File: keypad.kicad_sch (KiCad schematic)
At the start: 84 parts, among them J1 UJ20-C-H-G-SMT-5-P16-TR, SW1 SW_SPST, SW10 SW_SPST, SW11 SW_SPST, SW12 SW_SPST, SW13 SW_SPST, SW14 SW_SPST, SW15 SW_SPST, SW16 SW_SPST, SW17 SW_SPST, SW18 SW_SPST, SW19 SW_SPST, SW2 SW_SPST, SW20 SW_SPST, SW21 SW_SPST, SW22 SW_SPST, SW23 SW_SPST, SW24 SW_SPST, SW25 SW_SPST, SW26 SW_Reset, SW3 SW_SPST, SW4 SW_SPST, SW5 SW_SPST, SW6 SW_SPST, SW7 SW_SPST, SW8 SW_SPST, SW9 SW_SPST, U1 ATmega32U4-A, Y1 LFXTAL085842

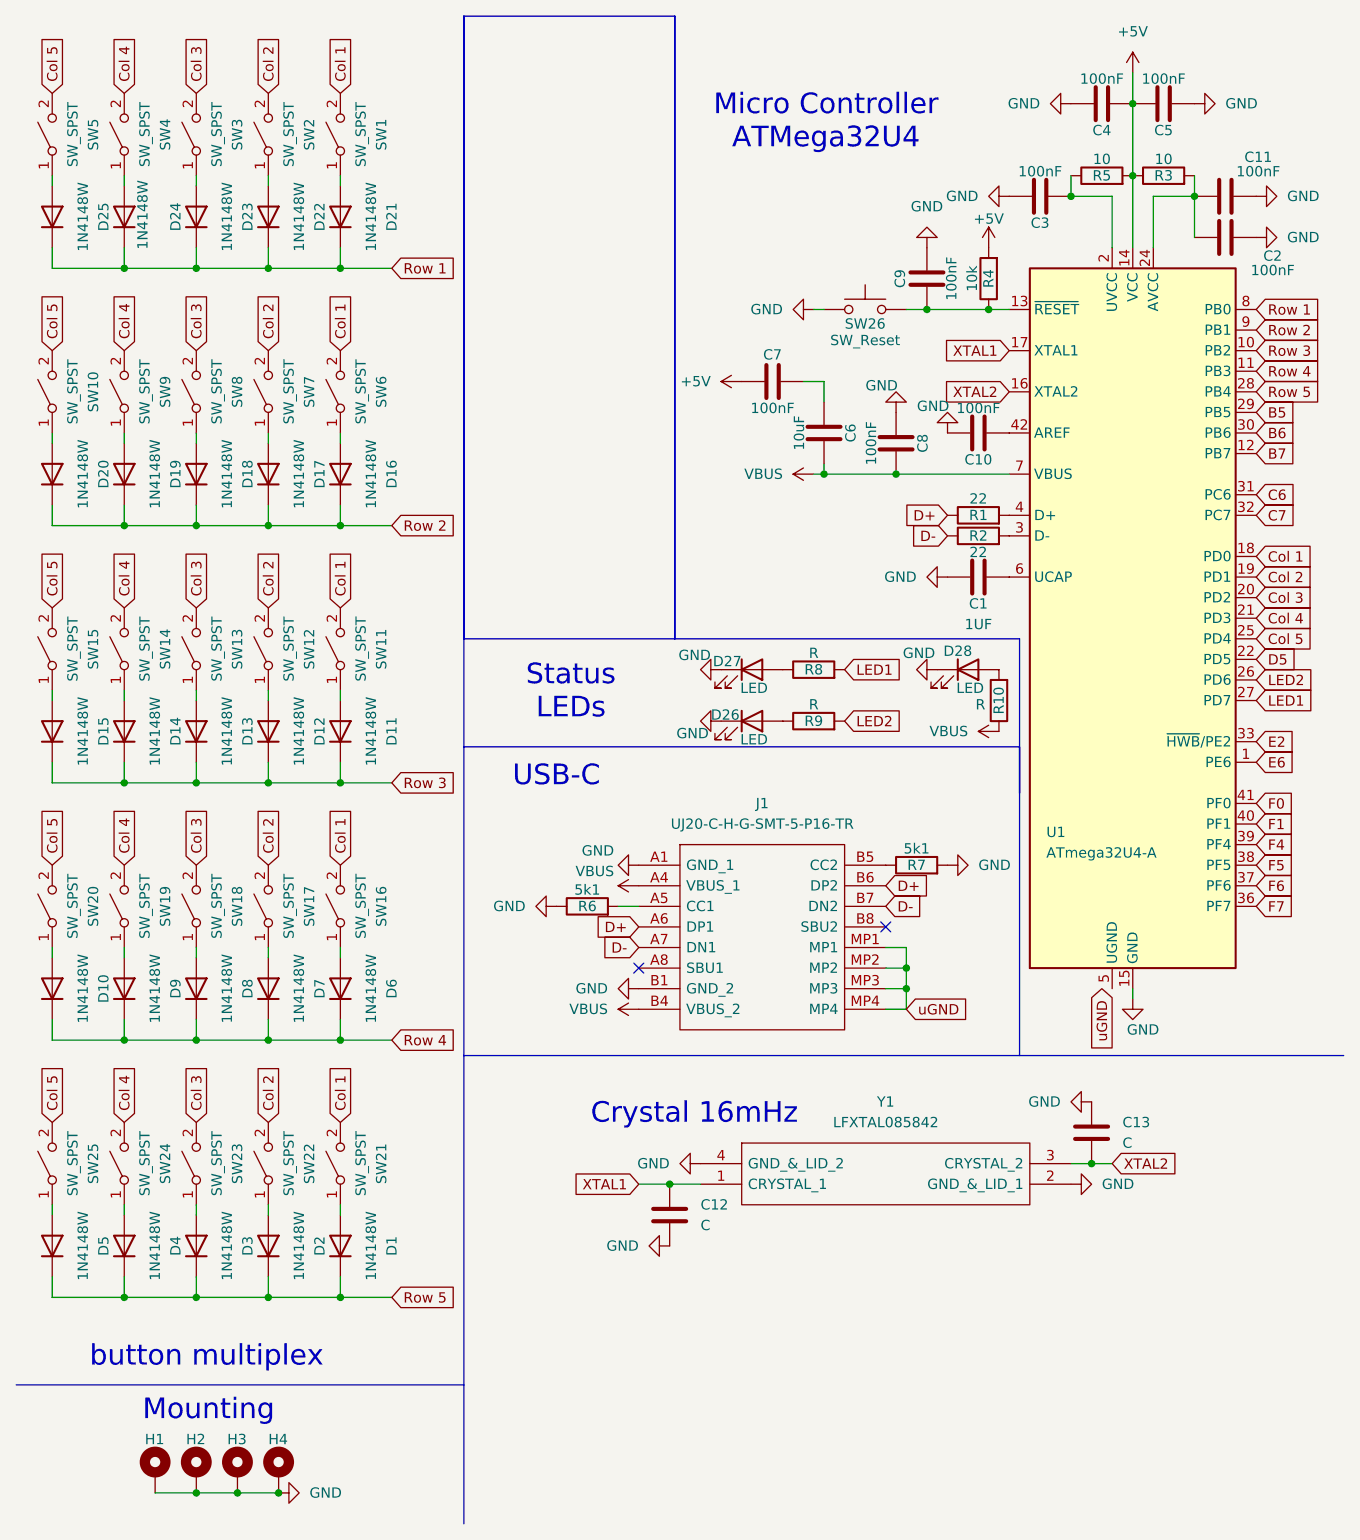
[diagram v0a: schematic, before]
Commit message: switched MC to QFN, rerouted board
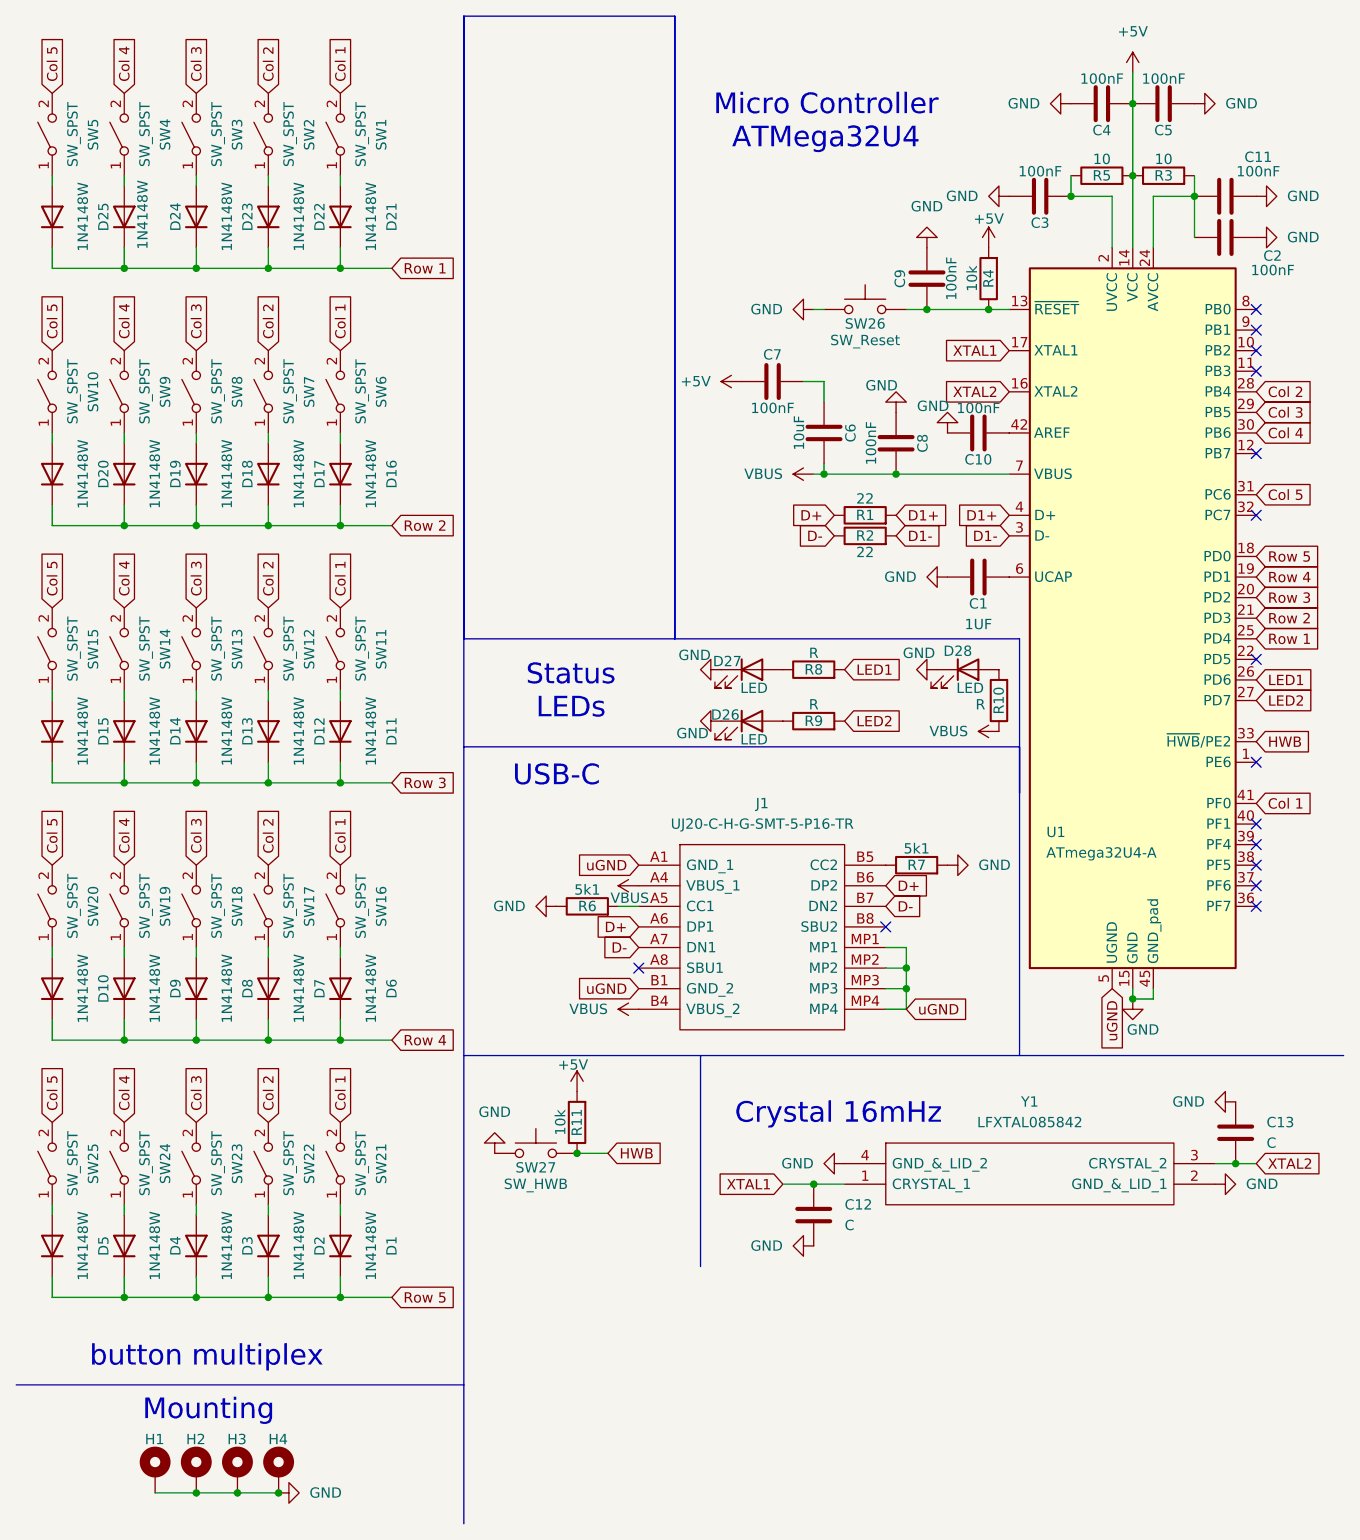
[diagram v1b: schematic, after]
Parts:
- added R11: 10k, Resistor_SMD:R_0603_1608Metric, symbol Device:R
- added SW27: SW_HWB, Button_Switch_SMD:SW_Push_1P1T_NO_CK_KSC7xxJ, symbol Switch:SW_Push
- U1: footprint Package_QFP:TQFP-44_10x10mm_P0.8mm -> Package_DFN_QFN:QFN-44-1EP_7x7mm_P0.5mm_EP5.15x5.15mm
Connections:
- net B5 is gone; now on net Col 3: U1.29 (PB5)
- net B6 is gone; now on net Col 4: U1.30 (PB6)
- net C6 is gone; now on net Col 5: U1.31 (PC6)
- net F0 is gone; now on net Col 1: U1.41 (PF0)
- net +5V: now also R11.2
- net Col 1: no longer U1.18 (PD0)
- net Col 2: now also U1.28 (PB4); no longer U1.19 (PD1)
- net Col 3: no longer U1.20 (PD2)
- net Col 4: no longer U1.21 (PD3)
- net Col 5: no longer U1.25 (PD4)
- net GND: now also U1.45 (GND_pad), SW27.1; no longer J1.A1 (GND_1), J1.B1 (GND_2)
- net LED1: now also U1.26 (PD6); no longer U1.27 (PD7)
- net LED2: now also U1.27 (PD7); no longer U1.26 (PD6)
- net Row 1: now also U1.25 (PD4); no longer U1.8 (PB0)
- net Row 2: now also U1.21 (PD3); no longer U1.9 (PB1)
- net Row 3: now also U1.20 (PD2); no longer U1.10 (PB2)
- net Row 4: now also U1.19 (PD1); no longer U1.11 (PB3)
- net Row 5: now also U1.18 (PD0); no longer U1.28 (PB4)
- net uGND: now also J1.A1 (GND_1), J1.B1 (GND_2), U1.5 (UGND)
- net D1-: now reaches R2.2, U1.3 (D-)
- net D1+: now reaches R1.2, U1.4 (D+)
- net B7: no longer names the net of U1.12 (PB7)
- net C7: no longer names the net of U1.32 (PC7)
- net D5: no longer names the net of U1.22 (PD5)
- net E2 renamed HWB
- net HWB: now also R11.1, SW27.2
- net E6: no longer names the net of U1.1 (PE6)
- net F1: no longer names the net of U1.40 (PF1)
- net F4: no longer names the net of U1.39 (PF4)
- net F5: no longer names the net of U1.38 (PF5)
- net F6: no longer names the net of U1.37 (PF6)
- net F7: no longer names the net of U1.36 (PF7)
- no-connect marks 2 -> 15
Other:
- title: (none) -> Macropad 5x5
- moved on the sheet: C12, C13, R1, R2, Y1
